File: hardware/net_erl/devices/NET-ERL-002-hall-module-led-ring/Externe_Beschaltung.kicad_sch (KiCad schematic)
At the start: 8 parts, among them SW1 SW_Push

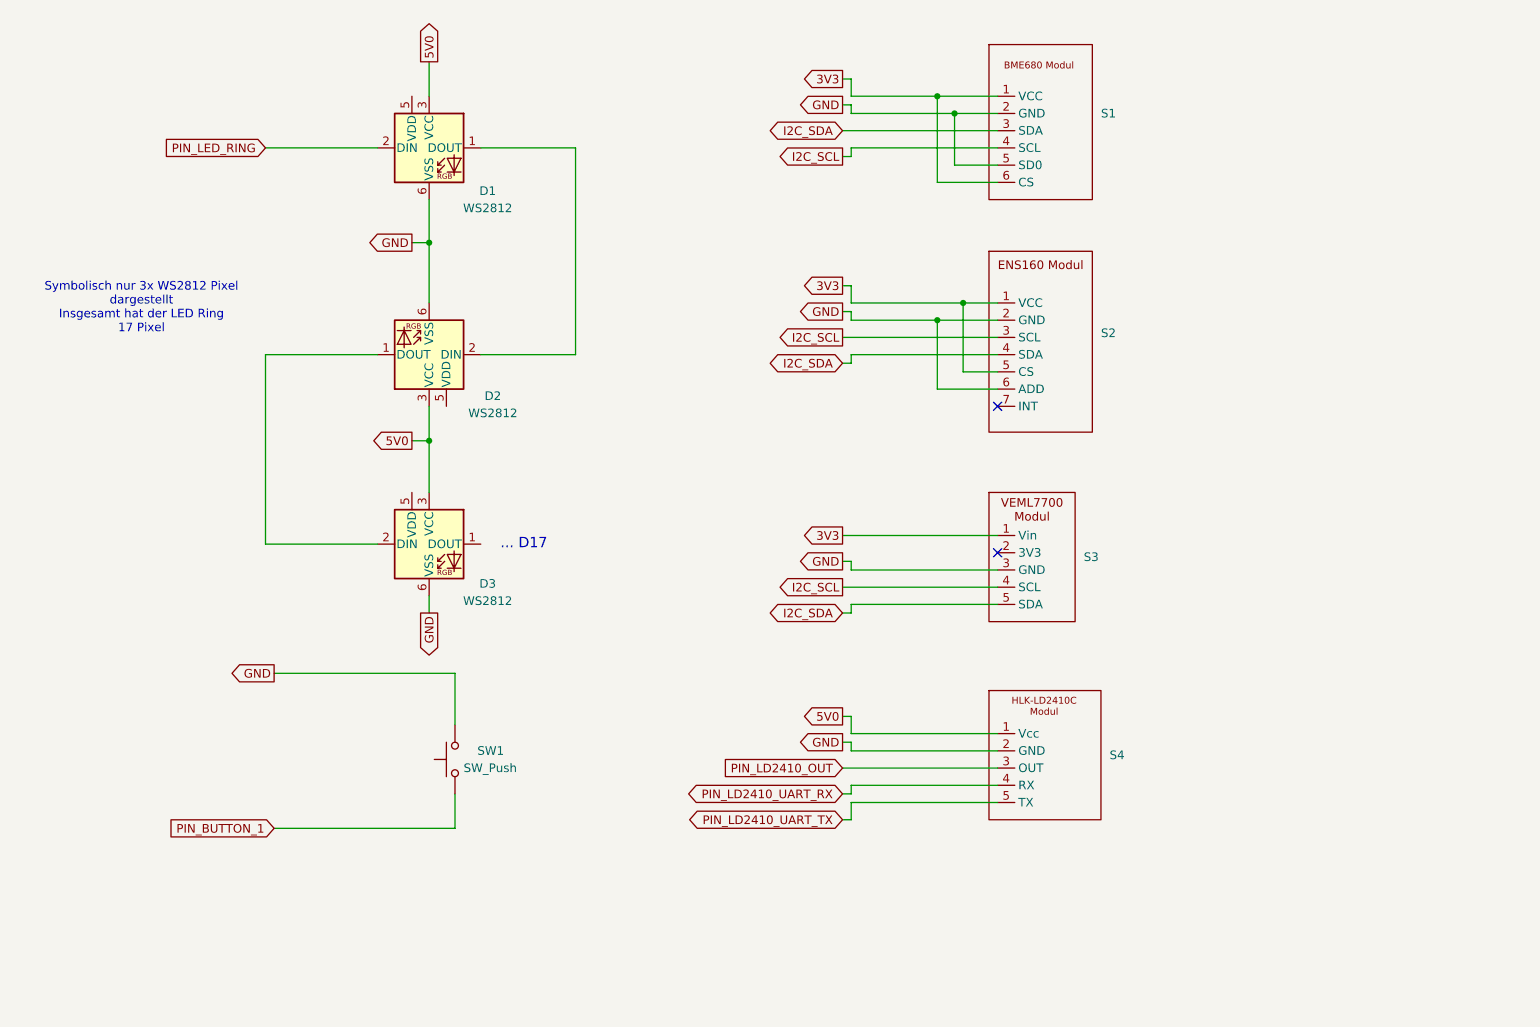
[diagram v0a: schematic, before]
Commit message: öffentliche Präsentation bereinigt: KI-Referenzen entfernt, READMEs optimiert, Firmware als Hauptlinie, ESPHome als Alternative mit Disclaimer
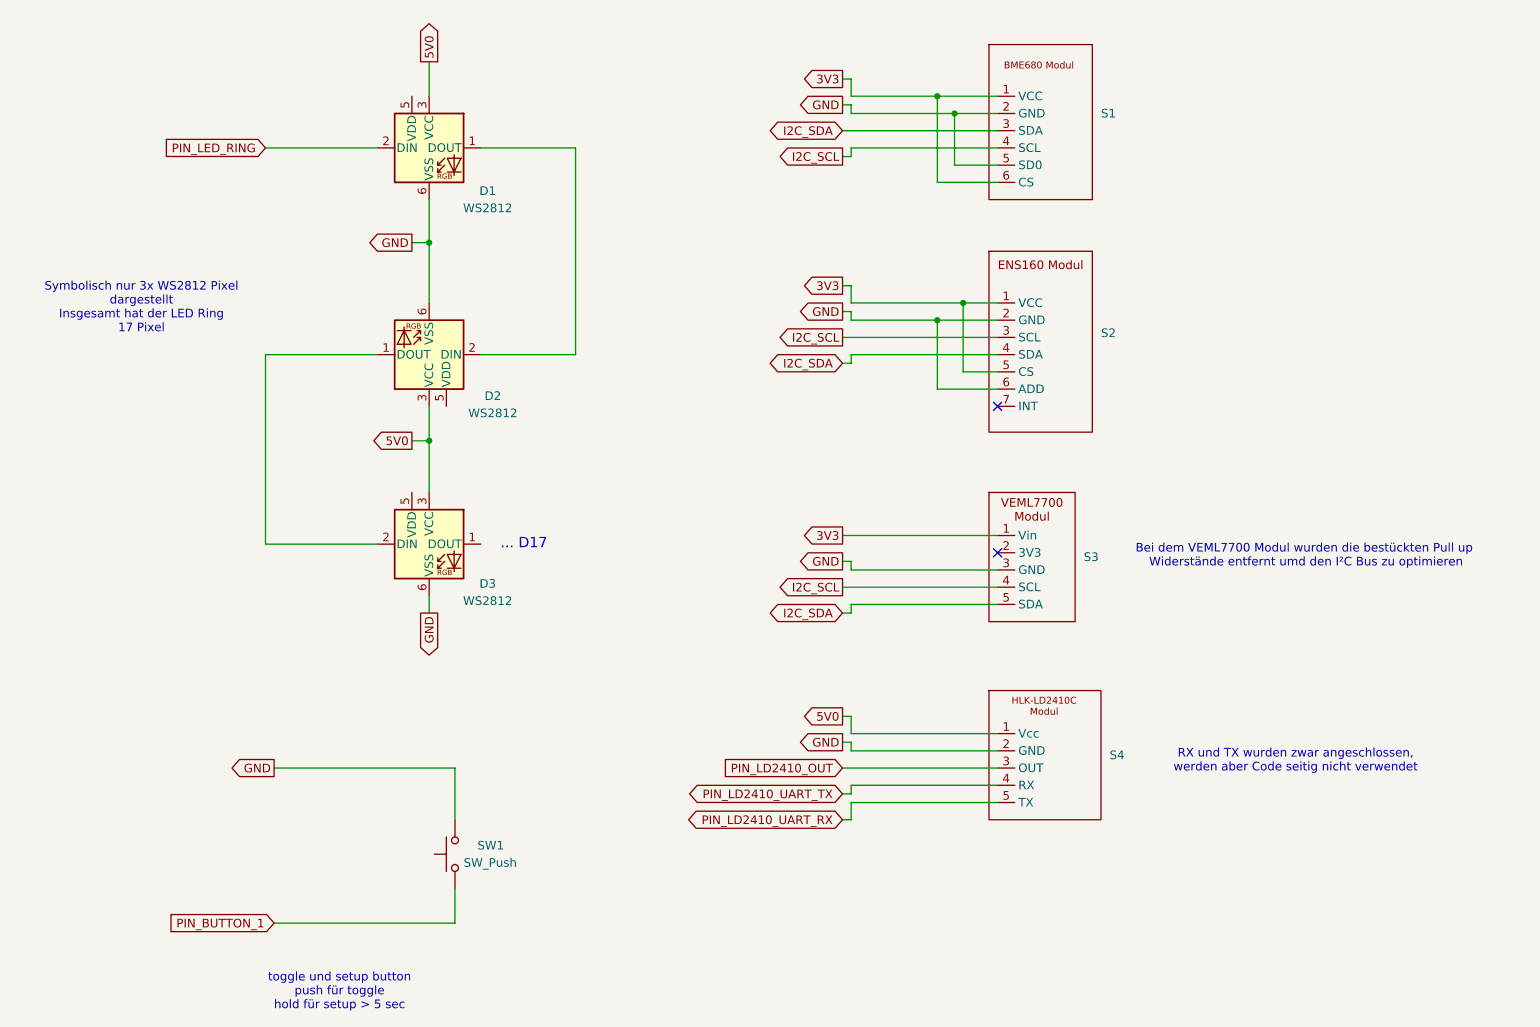
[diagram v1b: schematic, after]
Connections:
- net PIN_LD2410_UART_RX: now also S4.5 (TX); no longer S4.4 (RX)
- net PIN_LD2410_UART_TX: now also S4.4 (RX); no longer S4.5 (TX)
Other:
- note added: "Bei dem VEML7700 Modul wurden die bestückten Pull up Widerstände entfernt umd den I²C Bus zu optimieren"
- note added: "RX und TX wurden zwar angeschlossen, werden aber Code seitig nicht verwendet"
- note added: "toggle und setup button push für toggle hold für setup > 5 sec"
- moved on the sheet: SW1
